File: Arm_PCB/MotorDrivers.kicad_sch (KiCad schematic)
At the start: 54 parts, among them J19 Conn_02x03_Counter_Clockwise, J20 Conn_02x03_Counter_Clockwise, U1 TB6560_Board, U10 TB6560_Board, U11 INA219AxDCN, U12 TB6560_Board, U13 INA219AxDCN, U14 TB6560_Board, U15 INA219AxDCN, U16 TB6560_Board, U2 INA219AxDCN, U3 INA219AxDCN, U4 INA219AxDCN, U5 TB6560_Board, U6 INA219AxDCN, U7 TB6560_Board, U8 INA219AxDCN, U9 INA219AxDCN

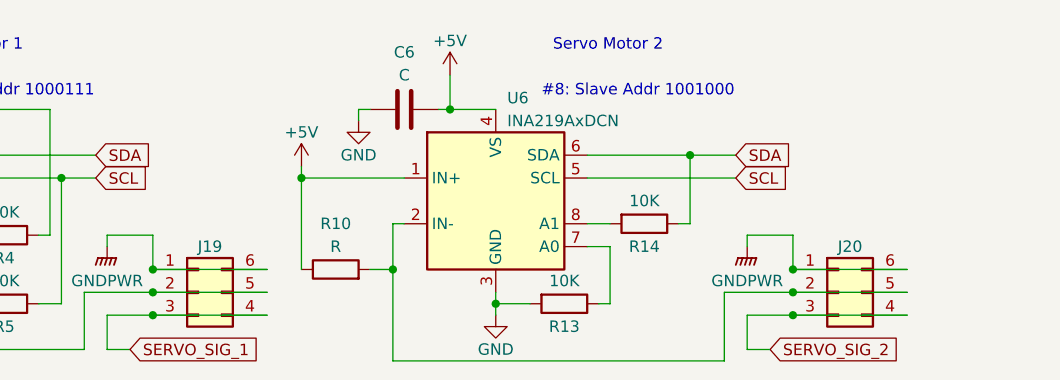
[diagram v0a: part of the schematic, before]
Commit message: Added a basic footprint for the PCB
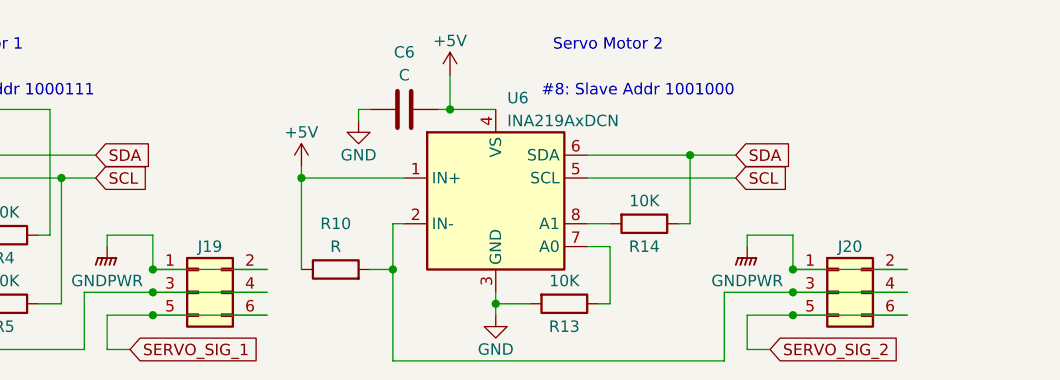
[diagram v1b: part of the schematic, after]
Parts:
- C1, C2, C3, C4, C5, C6, C7, C8, C9: footprint (none) -> Capacitor_SMD:C_1206_3216Metric_Pad1.33x1.80mm_HandSolder
- J19, J20: footprint (none) -> Connector_PinHeader_2.54mm:PinHeader_2x03_P2.54mm_Vertical; symbol Connector_Generic:Conn_02x03_Counter_Clockwise -> Connector_Generic:Conn_02x03_Odd_Even
- R1, R10, R11, R12, R13, R14, R15, R16, R17, R18, R19, R2, R20, R21, R22, R23, R24, R25, R26, R27, R3, R4, R5, R6, R7, R8, R9: footprint (none) -> Resistor_SMD:R_1206_3216Metric_Pad1.30x1.75mm_HandSolder
- U1, U10, U12, U14, U16, U5, U7: footprint (none) -> Arm_Footprints:TB6560_Breakout
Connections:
- net GNDPWR: now also J19.2 (Pin_2), J20.2 (Pin_2); no longer J19.6 (Pin_6), J20.6 (Pin_6)
- net SERVO_SIG_1: now also J19.5 (Pin_5), J19.6 (Pin_6); no longer J19.3 (Pin_3), J19.4 (Pin_4)
- net SERVO_SIG_2: now also J20.5 (Pin_5), J20.6 (Pin_6); no longer J20.3 (Pin_3), J20.4 (Pin_4)
- net at R10.2, U6.2 (IN-): now also J20.3 (Pin_3), J20.4 (Pin_4); no longer J20.2 (Pin_2), J20.5 (Pin_5)
- net at R1.2, U2.2 (IN-): now also J19.3 (Pin_3), J19.4 (Pin_4); no longer J19.2 (Pin_2), J19.5 (Pin_5)

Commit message: Continue layout, pick some components
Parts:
- C1, C2, C3, C4, C5, C6, C7, C8, C9: value C -> 0.1u
- R1, R10, R11, R12, R19, R2, R20, R25, R3: value R -> 2m
- U11, U13, U15, U2, U3, U4, U6, U8, U9: footprint Package_TO_SOT_SMD:SOT-23-8 -> Package_SO:SOIC-8_3.9x4.9mm_P1.27mm
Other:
- note added: "0.2 watt 10A"
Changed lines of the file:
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@@
+    (effects (font (size 1.27 1.27)) (justify left bottom))
+  )
+  (text "0.2 watt\n10A" (at 19.05 92.71 0)
     (effects (font (size 1.27 1.27)) (justify left bottom))
   )
@@
       (effects (font (size 1.27 1.27)) (justify left))
     )
-    (property "Footprint" "Package_TO_SOT_SMD:SOT-23-8" (at 125.73 190.5 0)
+    (property "Footprint" "Package_SO:SOIC-8_3.9x4.9mm_P1.27mm" (at 125.73 190.5 0)
       (effects (font (size 1.27 1.27)) hide)
     )
@@
       (effects (font (size 1.27 1.27)))
     )
-    (property "Value" "C" (at 91.44 71.12 90)
+    (property "Value" "0.1u" (at 91.44 71.12 90)
       (effects (font (size 1.27 1.27)))
     )
@@
       (effects (font (size 1.27 1.27)))
     )
-    (property "Value" "C" (at 217.17 81.28 90)
+    (property "Value" "0.1u" (at 217.17 81.28 90)
       (effects (font (size 1.27 1.27)))
     )
@@
       (effects (font (size 1.27 1.27)) (justify left))
     )
-    (property "Footprint" "Package_TO_SOT_SMD:SOT-23-8" (at 127 93.98 0)
+    (property "Footprint" "Package_SO:SOIC-8_3.9x4.9mm_P1.27mm" (at 127 93.98 0)
       (effects (font (size 1.27 1.27)) hide)
     )
@@
       (effects (font (size 1.27 1.27)))
     )
-    (property "Value" "R" (at 154.94 93.98 90)
+    (property "Value" "2m" (at 154.94 93.98 90)
       (effects (font (size 1.27 1.27)))
     )
@@
       (effects (font (size 1.27 1.27)) (justify left))
     )
-    (property "Footprint" "Package_TO_SOT_SMD:SOT-23-8" (at 62.23 138.43 0)
+    (property "Footprint" "Package_SO:SOIC-8_3.9x4.9mm_P1.27mm" (at 62.23 138.43 0)
       (effects (font (size 1.27 1.27)) hide)
     )
@@
       (effects (font (size 1.27 1.27)))
     )
-    (property "Value" "10K" (at 72.39 91.44 90)
+    (property "Value" "10K" (at 72.39 83.82 90)
       (effects (font (size 1.27 1.27)))
     )
@@
       (effects (font (size 1.27 1.27)))
     )
-    (property "Value" "C" (at 99.06 167.64 90)
+    (property "Value" "0.1u" (at 99.06 167.64 90)
       (effects (font (size 1.27 1.27)))
     )
@@
   )
   (symbol (lib_id "Device:C") (at 96.52 119.38 270) (unit 1)
-    (in_bom yes) (on_board yes) (dnp no) (fields_autoplaced)
-    (property "Reference" "C5" (at 96.52 111.76 90)
-      (effects (font (size 1.27 1.27)))
-    )
-    (property "Value" "C" (at 96.52 114.3 90)
+    (in_bom yes) (on_board yes) (dnp no)
+    (property "Reference" "C5" (at 96.52 113.03 90)
+      (effects (font (size 1.27 1.27)))
+    )
+    (property "Value" "0.1u" (at 96.52 115.57 90)
       (effects (font (size 1.27 1.27)))
     )
@@
       (effects (font (size 1.27 1.27)) (justify left))
     )
-    (property "Footprint" "Package_TO_SOT_SMD:SOT-23-8" (at 63.5 92.71 0)
+    (property "Footprint" "Package_SO:SOIC-8_3.9x4.9mm_P1.27mm" (at 63.5 92.71 0)
       (effects (font (size 1.27 1.27)) hide)
     )
@@
       (effects (font (size 1.27 1.27)))
     )
-    (property "Value" "R" (at 97.79 134.62 90)
+    (property "Value" "2m" (at 97.79 134.62 90)
       (effects (font (size 1.27 1.27)))
     )
@@
       (effects (font (size 1.27 1.27)))
     )
-    (property "Value" "R" (at 26.67 134.62 90)
+    (property "Value" "2m" (at 26.67 134.62 90)
       (effects (font (size 1.27 1.27)))
     )
@@
       (effects (font (size 1.27 1.27)) (justify left))
     )
-    (property "Footprint" "Package_TO_SOT_SMD:SOT-23-8" (at 187.96 97.79 0)
+    (property "Footprint" "Package_SO:SOIC-8_3.9x4.9mm_P1.27mm" (at 187.96 97.79 0)
       (effects (font (size 1.27 1.27)) hide)
     )
@@
       (effects (font (size 1.27 1.27)))
     )
-    (property "Value" "R" (at 20.32 186.69 90)
+    (property "Value" "2m" (at 20.32 186.69 90)
       (effects (font (size 1.27 1.27)))
     )
@@
       (effects (font (size 1.27 1.27)) (justify left))
     )
-    (property "Footprint" "Package_TO_SOT_SMD:SOT-23-8" (at 195.58 140.97 0)
+    (property "Footprint" "Package_SO:SOIC-8_3.9x4.9mm_P1.27mm" (at 195.58 140.97 0)
       (effects (font (size 1.27 1.27)) hide)
     )
@@
       (effects (font (size 1.27 1.27)))
     )
-    (property "Value" "C" (at 27.94 167.64 90)
+    (property "Value" "0.1u" (at 27.94 167.64 90)
       (effects (font (size 1.27 1.27)))
     )
@@
       (effects (font (size 1.27 1.27)))
     )
-    (property "Value" "R" (at 214.63 100.33 90)
+    (property "Value" "2m" (at 214.63 100.33 90)
       (effects (font (size 1.27 1.27)))
     )
@@
       (effects (font (size 1.27 1.27)))
     )
-    (property "Value" "10K" (at 72.39 83.82 90)
+    (property "Value" "10K" (at 72.39 91.44 90)
       (effects (font (size 1.27 1.27)))
     )
@@
       (effects (font (size 1.27 1.27)) (justify left))
     )
-    (property "Footprint" "Package_TO_SOT_SMD:SOT-23-8" (at 54.61 190.5 0)
+    (property "Footprint" "Package_SO:SOIC-8_3.9x4.9mm_P1.27mm" (at 54.61 190.5 0)
       (effects (font (size 1.27 1.27)) hide)
     )
@@
       (effects (font (size 1.27 1.27)) (justify left))
     )
-    (property "Footprint" "Package_TO_SOT_SMD:SOT-23-8" (at 132.08 138.43 0)
+    (property "Footprint" "Package_SO:SOIC-8_3.9x4.9mm_P1.27mm" (at 132.08 138.43 0)
       (effects (font (size 1.27 1.27)) hide)
     )
@@
       (effects (font (size 1.27 1.27)))
     )
-    (property "Value" "R" (at 91.44 186.69 90)
+    (property "Value" "2m" (at 91.44 186.69 90)
       (effects (font (size 1.27 1.27)))
     )
@@
       (effects (font (size 1.27 1.27)))
     )
-    (property "Value" "C" (at 165.1 118.11 90)
+    (property "Value" "0.1u" (at 165.1 118.11 90)
       (effects (font (size 1.27 1.27)))
     )
@@
   )
   (symbol (lib_id "Device:C") (at 26.67 119.38 270) (unit 1)
-    (in_bom yes) (on_board yes) (dnp no) (fields_autoplaced)
-    (property "Reference" "C1" (at 26.67 111.76 90)
-      (effects (font (size 1.27 1.27)))
-    )
-    (property "Value" "C" (at 26.67 114.3 90)
+    (in_bom yes) (on_board yes) (dnp no)
+    (property "Reference" "C1" (at 26.67 113.03 90)
+      (effects (font (size 1.27 1.27)))
+    )
+    (property "Value" "0.1u" (at 26.67 115.57 90)
       (effects (font (size 1.27 1.27)))
     )
@@
       (effects (font (size 1.27 1.27)))
     )
-    (property "Value" "R" (at 31.75 88.9 90)
+    (property "Value" "2m" (at 31.75 88.9 90)
       (effects (font (size 1.27 1.27)))
     )
@@
   )
   (symbol (lib_id "power:+5V") (at 36.83 115.57 0) (unit 1)
-    (in_bom yes) (on_board yes) (dnp no) (fields_autoplaced)
+    (in_bom yes) (on_board yes) (dnp no)
     (property "Reference" "#PWR027" (at 36.83 119.38 0)
       (effects (font (size 1.27 1.27)) hide)
     )
-    (property "Value" "+5V" (at 36.83 110.49 0)
+    (property "Value" "+5V" (at 36.83 111.76 0)
       (effects (font (size 1.27 1.27)))
     )
@@
       (effects (font (size 1.27 1.27)) (justify left))
     )
-    (property "Footprint" "Package_TO_SOT_SMD:SOT-23-8" (at 248.92 104.14 0)
+    (property "Footprint" "Package_SO:SOIC-8_3.9x4.9mm_P1.27mm" (at 248.92 104.14 0)
       (effects (font (size 1.27 1.27)) hide)
     )
@@
       (effects (font (size 1.27 1.27)))
     )
-    (property "Value" "C" (at 157.48 74.93 90)
+    (property "Value" "0.1u" (at 157.48 74.93 90)
       (effects (font (size 1.27 1.27)))
     )
@@
   )
   (symbol (lib_id "Device:C") (at 27.94 73.66 270) (unit 1)
-    (in_bom yes) (on_board yes) (dnp no) (fields_autoplaced)
-    (property "Reference" "C2" (at 27.94 66.04 90)
-      (effects (font (size 1.27 1.27)))
-    )
-    (property "Value" "C" (at 27.94 68.58 90)
+    (in_bom yes) (on_board yes) (dnp no)
+    (property "Reference" "C2" (at 27.94 67.31 90)
+      (effects (font (size 1.27 1.27)))
+    )
+    (property "Value" "0.1u" (at 27.94 69.85 90)
       (effects (font (size 1.27 1.27)))
     )
@@
       (effects (font (size 1.27 1.27)))
     )
-    (property "Value" "R" (at 93.98 90.17 90)
+    (property "Value" "2m" (at 93.98 90.17 90)
       (effects (font (size 1.27 1.27)))
     )
@@
       (effects (font (size 1.27 1.27)))
     )
-    (property "Value" "R" (at 161.29 137.16 90)
-      (effects (font (size 1.27 1.27)))
-    )
+    (property "Value" "2m" (at 161.29 137.16 90)
+      (effects (font (size 1.27 1.27)))
+    )

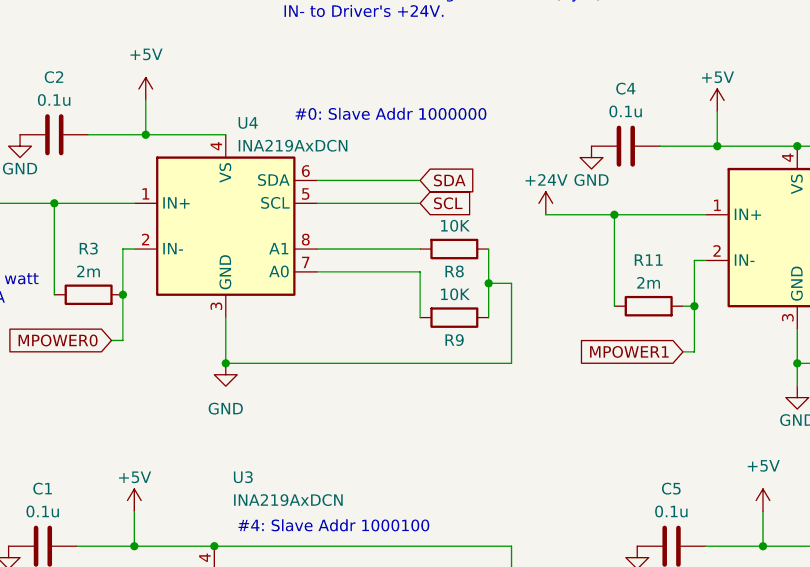
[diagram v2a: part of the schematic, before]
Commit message: Footprint updates with new TB6600
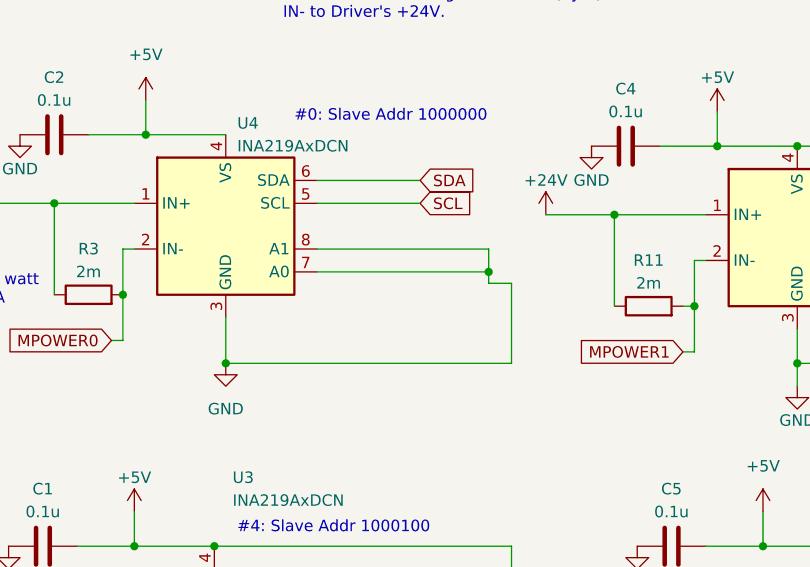
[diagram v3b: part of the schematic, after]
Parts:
- removed R8, R9: 10K, Resistor_SMD:R_1206_3216Metric_Pad1.30x1.75mm_HandSolder, symbol Device:R
- U1, U16: footprint Arm_Footprints:TB6560_Breakout -> Arm_Footprints:TB6600_Breakout
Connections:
- net GND: now also U4.7 (A0), U4.8 (A1)
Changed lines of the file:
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@@
   (junction (at 125.73 43.18) (diameter 0) (color 0 0 0 0)
   )
+  (junction (at 76.2 88.9) (diameter 0) (color 0 0 0 0)
+  )
   (junction (at 160.02 96.52) (diameter 0) (color 0 0 0 0)
   )
@@
   (junction (at 71.12 194.31) (diameter 0) (color 0 0 0 0)
   )
-  (junction (at 76.2 90.17) (diameter 0) (color 0 0 0 0)
-  )
   (junction (at 106.68 119.38) (diameter 0) (color 0 0 0 0)
   )
@@
     (stroke (width 0) (type default))
   )
+  (wire (pts (xy 76.2 88.9) (xy 76.2 90.17))
+    (stroke (width 0) (type default))
+  )
   (wire (pts (xy 96.52 16.51) (xy 97.79 16.51))
     (stroke (width 0) (type default))
@@
     (stroke (width 0) (type default))
   )
-  (wire (pts (xy 57.15 86.36) (xy 68.58 86.36))
+  (wire (pts (xy 57.15 86.36) (xy 76.2 86.36))
     (stroke (width 0) (type default))
   )
@@
     (stroke (width 0) (type default))
   )
-  (wire (pts (xy 76.2 86.36) (xy 76.2 90.17))
+  (wire (pts (xy 76.2 86.36) (xy 76.2 88.9))
     (stroke (width 0) (type default))
   )
@@
     (stroke (width 0) (type default))
   )
-  (wire (pts (xy 57.15 88.9) (xy 68.58 88.9))
+  (wire (pts (xy 57.15 88.9) (xy 76.2 88.9))
     (stroke (width 0) (type default))
   )
@@
     (stroke (width 0) (type default))
   )
-  (wire (pts (xy 76.2 90.17) (xy 76.2 93.98))
-    (stroke (width 0) (type default))
-  )
   (wire (pts (xy 196.85 102.87) (xy 171.45 102.87))
     (stroke (width 0) (type default))
@@
     (stroke (width 0) (type default))
   )
-  (wire (pts (xy 68.58 88.9) (xy 68.58 93.98))
-    (stroke (width 0) (type default))
-  )
   (text "#1: Slave Addr 1000001" (at 118.11 73.66 0)
     (effects (font (size 1.27 1.27)) (justify left bottom))
@@
     )
   )
-  (symbol (lib_id "Device:R") (at 72.39 86.36 270) (unit 1)
-    (in_bom yes) (on_board yes) (dnp no)
-    (property "Reference" "R8" (at 72.39 88.9 90)
-      (effects (font (size 1.27 1.27)))
-    )
-    (property "Value" "10K" (at 72.39 83.82 90)
-      (effects (font (size 1.27 1.27)))
-    )
-    (property "Footprint" "Resistor_SMD:R_1206_3216Metric_Pad1.30x1.75mm_HandSolder" (at 72.39 84.582 90)
-      (effects (font (size 1.27 1.27)) hide)
-    )
-    (property "Datasheet" "~" (at 72.39 86.36 0)
-      (effects (font (size 1.27 1.27)) hide)
-    )
-    (pin "1")
-    (pin "2")
-    (instances
-      (project "Arm_PCB"
-        (path "/f8b9fbb1-757f-4aa8-8e30-7f83a30c7c5f/bb228902-3eef-4db7-9bf2-e6e1028f63fe"
-          (reference "R8") (unit 1)
-        )
-      )
-    )
-  )
   (symbol (lib_id "power:GNDPWR") (at 236.22 40.64 0) (unit 1)
     (in_bom yes) (on_board yes) (dnp no)
@@
       (effects (font (size 1.27 1.27)))
     )
-    (property "Footprint" "Arm_Footprints:TB6560_Breakout" (at 13.97 33.02 0)
+    (property "Footprint" "Arm_Footprints:TB6600_Breakout" (at 13.97 33.02 0)
       (effects (font (size 1.27 1.27)) hide)
     )
@@
     )
   )
-  (symbol (lib_id "Device:R") (at 72.39 93.98 270) (unit 1)
-    (in_bom yes) (on_board yes) (dnp no)
-    (property "Reference" "R9" (at 72.39 96.52 90)
-      (effects (font (size 1.27 1.27)))
-    )
-    (property "Value" "10K" (at 72.39 91.44 90)
-      (effects (font (size 1.27 1.27)))
-    )
-    (property "Footprint" "Resistor_SMD:R_1206_3216Metric_Pad1.30x1.75mm_HandSolder" (at 72.39 92.202 90)
-      (effects (font (size 1.27 1.27)) hide)
-    )
-    (property "Datasheet" "~" (at 72.39 93.98 0)
-      (effects (font (size 1.27 1.27)) hide)
-    )
-    (pin "1")
-    (pin "2")
-    (instances
-      (project "Arm_PCB"
-        (path "/f8b9fbb1-757f-4aa8-8e30-7f83a30c7c5f/bb228902-3eef-4db7-9bf2-e6e1028f63fe"
-          (reference "R9") (unit 1)
-        )
-      )
-    )
-  )
   (symbol (lib_id "Sensor_Energy:INA219AxDCN") (at 38.1 181.61 0) (unit 1)
     (in_bom yes) (on_board yes) (dnp no)
@@
       (effects (font (size 1.27 1.27)))
     )
-    (property "Footprint" "Arm_Footprints:TB6560_Breakout" (at 232.41 52.07 0)
+    (property "Footprint" "Arm_Footprints:TB6600_Breakout" (at 232.41 52.07 0)
       (effects (font (size 1.27 1.27)) hide)
     )
